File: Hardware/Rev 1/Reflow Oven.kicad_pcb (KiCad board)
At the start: 2 copper layers, 100 x 50 mm, 84 parts, among them IC1 MCP1792T, J1 SW, J10 2350513-2, J11 USB4110-GF-A_REVB, J12 POW_SEL, J13 Conn_01x02, J2 ENC, J3 Adafruit 4101, J4 Adafruit 4101, J5 Adafruit 4101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

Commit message: added date
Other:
- board text added: "June 2023"
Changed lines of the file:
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@@
     (effects (font (size 1 1) (thickness 0.15)) (justify left bottom))
+  )
+  (gr_text "June 2023" (at 193.75 83.75 90) (layer "B.Mask")
+    (effects (font (size 1 1) (thickness 0.15)) (justify left bottom mirror))
   )
   (dimension (type aligned) (layer "Eco1.User")

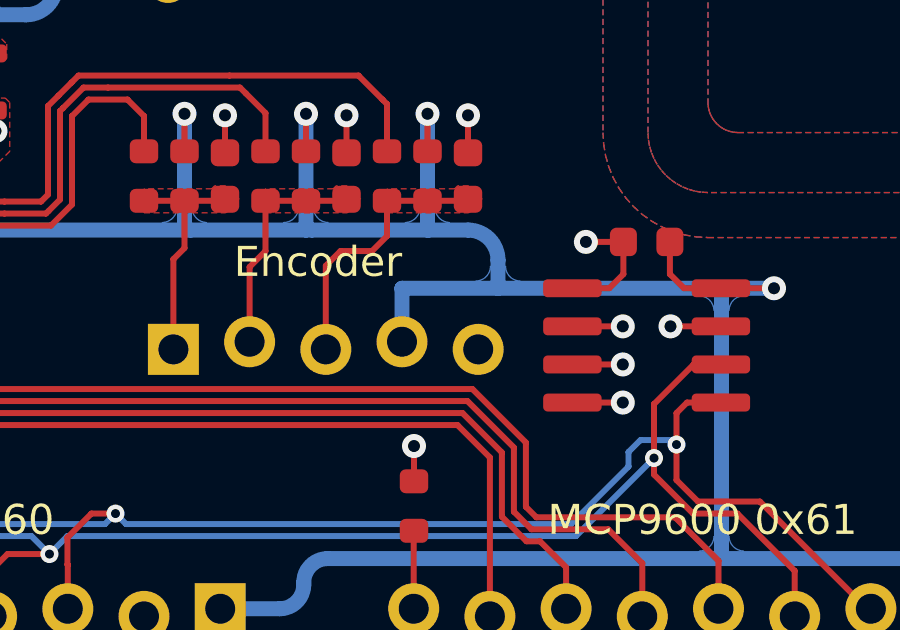
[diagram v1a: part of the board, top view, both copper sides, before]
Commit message: added missing teardrops
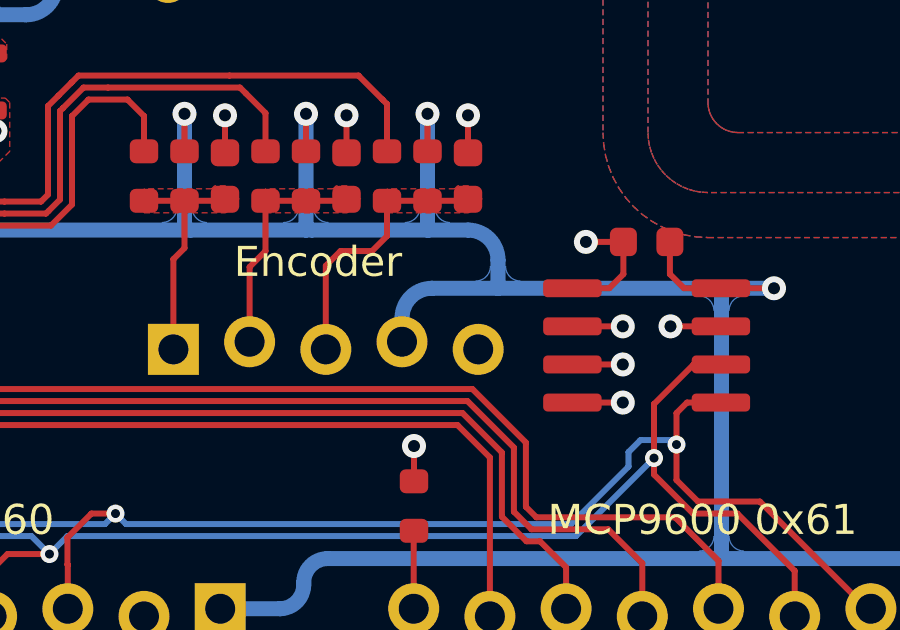
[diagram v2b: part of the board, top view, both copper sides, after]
